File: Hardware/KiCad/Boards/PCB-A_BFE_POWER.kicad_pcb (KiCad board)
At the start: 2 copper layers, 110 x 94 mm, 0 parts

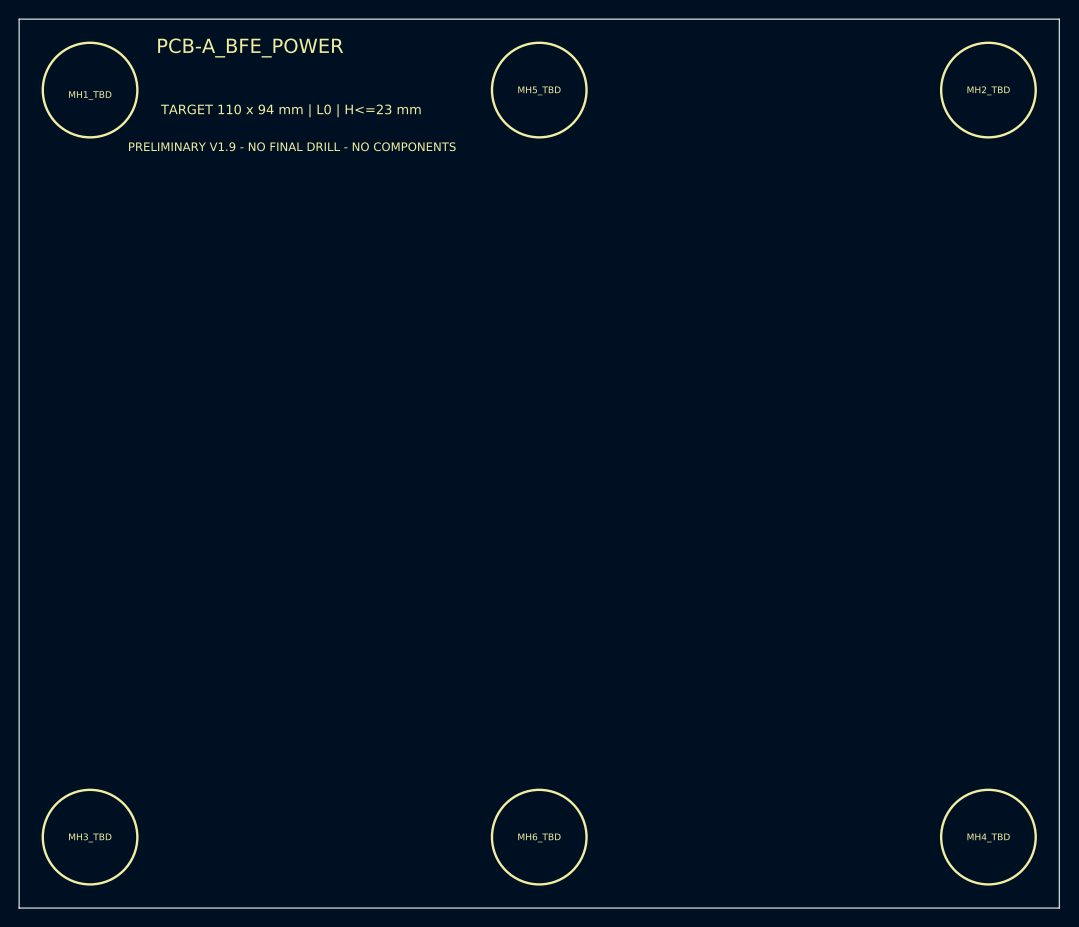
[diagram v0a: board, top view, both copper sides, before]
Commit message: hardware: add PCB-A functional and height placeholders
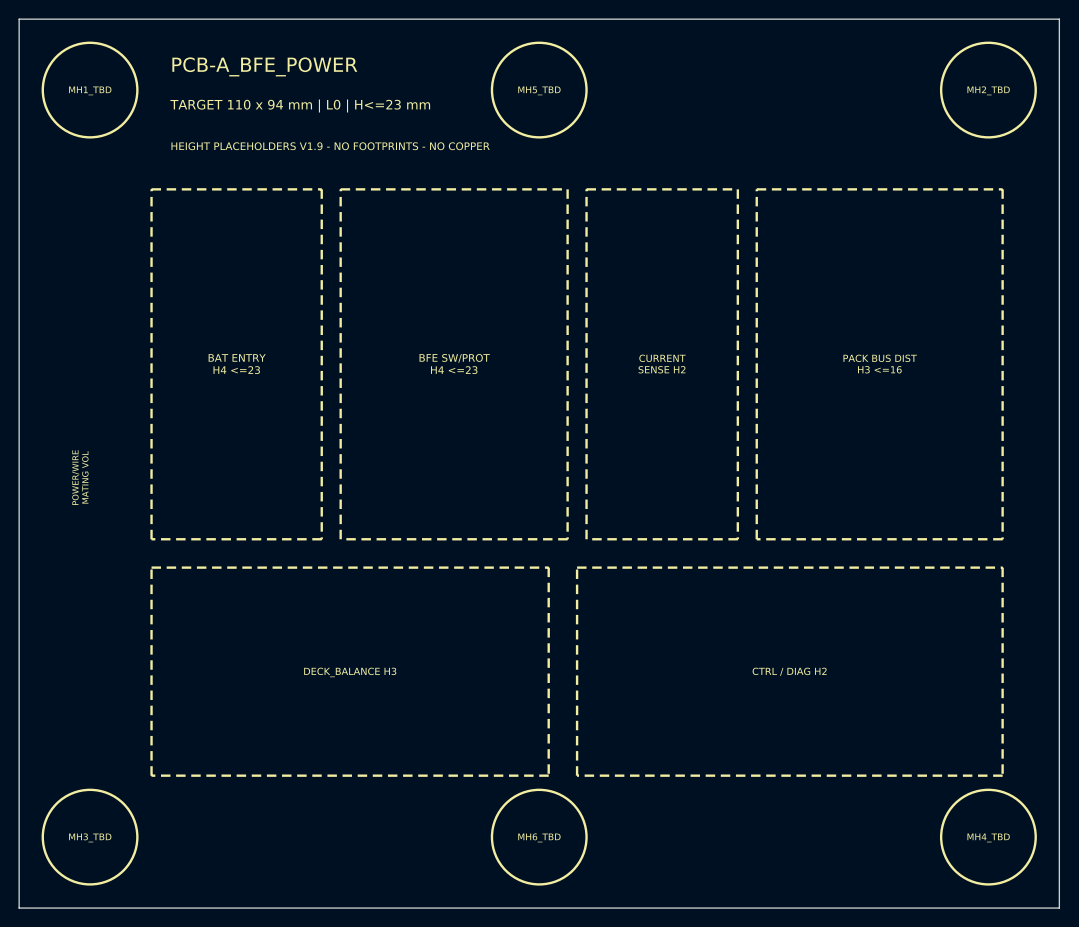
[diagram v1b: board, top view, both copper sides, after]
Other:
- board text added: "BAT ENTRY H4 <=23"
- board text added: "BFE SW/PROT H4 <=23"
- board text added: "CTRL / DIAG H2"
- board text added: "CURRENT SENSE H2"
- board text added: "DECK_BALANCE H3"
- board text added: "HEIGHT PLACEHOLDERS V1.9 - NO FOOTPRINTS - NO COPPER"
- board text added: "PACK BUS DIST H3 <=16"
- board text added: "POWER/WIRE MATING VOL"
- board text removed: "PRELIMINARY V1.9 - NO FINAL DRILL - NO COMPONENTS"
